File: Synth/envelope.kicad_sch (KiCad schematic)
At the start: 20 parts, among them U10 LM321, U7 LM321, U8 LM321, U9 LM321

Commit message: added some footprints
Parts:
- C5, C6: value C_Small -> 1uF; footprint (none) -> Capacitor_SMD:C_0805_2012Metric
- D1: value D -> 100k; footprint (none) -> Diode_SMD:D_0805_2012Metric
- D2, D3, D4, D5: footprint (none) -> Diode_SMD:D_0805_2012Metric
- R19: value R -> 10k; footprint (none) -> Resistor_SMD:R_0805_2012Metric
- R20, R21, R23: value R -> 100k; footprint (none) -> Resistor_SMD:R_0805_2012Metric
- R22: value R -> 47k; footprint (none) -> Resistor_SMD:R_0805_2012Metric
- R24: value R -> 1k; footprint (none) -> Resistor_SMD:R_0805_2012Metric
- RV10: value R_Potentiometer -> 1M
- RV9: value R_Potentiometer -> 100k
- renumbered RV11 to 1M1
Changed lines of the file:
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@@
   (symbol (lib_id "Device:R_Potentiometer") (at 175.26 108.585 270) (unit 1)
     (in_bom yes) (on_board yes) (dnp no)
-    (property "Reference" "RV11" (at 175.26 102.235 90)
+    (property "Reference" "1M1" (at 175.26 102.235 90)
       (effects (font (size 1.27 1.27)))
     )
@@
       (project "Synth"
         (path "/69caad27-d98a-4cdc-abd0-794bd5e6ba79/f75ed15d-dc0c-437e-bd82-524bc7e88f27"
-          (reference "RV11") (unit 1)
+          (reference "1M1") (unit 1)
         )
       )
@@
       (effects (font (size 1.27 1.27)))
     )
-    (property "Footprint" "" (at 167.64 108.585 0)
+    (property "Footprint" "Diode_SMD:D_0805_2012Metric" (at 167.64 108.585 0)
       (effects (font (size 1.27 1.27)) hide)
     )
@@
   (symbol (lib_id "Device:R_Potentiometer") (at 132.08 126.365 90) (unit 1)
     (in_bom yes) (on_board yes) (dnp no) (fields_autoplaced)
-    (property "Reference" "RV9" (at 132.08 130.175 90)
-      (effects (font (size 1.27 1.27)))
-    )
-    (property "Value" "R_Potentiometer" (at 132.08 132.715 90)
+    (property "Reference" "RV9" (at 132.08 129.54 90)
+      (effects (font (size 1.27 1.27)))
+    )
+    (property "Value" "100k" (at 132.08 132.08 90)
       (effects (font (size 1.27 1.27)))
     )
@@
       (effects (font (size 1.27 1.27)) (justify left))
     )
-    (property "Value" "R" (at 69.85 102.235 0)
+    (property "Value" "10k" (at 69.85 102.235 0)
       (effects (font (size 1.27 1.27)) (justify left))
     )
-    (property "Footprint" "" (at 66.167 100.965 90)
+    (property "Footprint" "Resistor_SMD:R_0805_2012Metric" (at 66.167 100.965 90)
       (effects (font (size 1.27 1.27)) hide)
     )
@@
       (effects (font (size 1.27 1.27)))
     )
-    (property "Value" "R" (at 89.535 114.935 90)
-      (effects (font (size 1.27 1.27)))
-    )
-    (property "Footprint" "" (at 89.535 114.173 90)
+    (property "Value" "100k" (at 89.535 114.935 90)
+      (effects (font (size 1.27 1.27)))
+    )
+    (property "Footprint" "Resistor_SMD:R_0805_2012Metric" (at 89.535 114.173 90)
       (effects (font (size 1.27 1.27)) hide)
     )
@@
       (effects (font (size 1.27 1.27)) (justify right))
     )
-    (property "Value" "C_Small" (at 198.12 102.8636 0)
+    (property "Value" "1uF" (at 198.12 102.8636 0)
       (effects (font (size 1.27 1.27)) (justify right))
     )
-    (property "Footprint" "" (at 195.58 101.6 0)
+    (property "Footprint" "Capacitor_SMD:C_0805_2012Metric" (at 195.58 101.6 0)
       (effects (font (size 1.27 1.27)) hide)
     )
@@
       (effects (font (size 1.27 1.27)))
     )
-    (property "Footprint" "" (at 123.19 98.425 0)
+    (property "Footprint" "Diode_SMD:D_0805_2012Metric" (at 123.19 98.425 0)
       (effects (font (size 1.27 1.27)) hide)
     )
@@
   (symbol (lib_id "Device:R") (at 106.68 112.395 90) (unit 1)
     (in_bom yes) (on_board yes) (dnp no) (fields_autoplaced)
-    (property "Reference" "R22" (at 106.68 106.045 90)
-      (effects (font (size 1.27 1.27)))
-    )
-    (property "Value" "R" (at 106.68 108.585 90)
-      (effects (font (size 1.27 1.27)))
-    )
-    (property "Footprint" "" (at 106.68 114.173 90)
+    (property "Reference" "R22" (at 106.68 106.68 90)
+      (effects (font (size 1.27 1.27)))
+    )
+    (property "Value" "47k" (at 106.68 109.22 90)
+      (effects (font (size 1.27 1.27)))
+    )
+    (property "Footprint" "Resistor_SMD:R_0805_2012Metric" (at 106.68 114.173 90)
       (effects (font (size 1.27 1.27)) hide)
     )
@@
       (effects (font (size 1.27 1.27)))
     )
-    (property "Footprint" "" (at 123.19 126.365 0)
+    (property "Footprint" "Diode_SMD:D_0805_2012Metric" (at 123.19 126.365 0)
       (effects (font (size 1.27 1.27)) hide)
     )
@@
       (effects (font (size 1.27 1.27)))
     )
-    (property "Footprint" "" (at 167.64 83.185 0)
+    (property "Footprint" "Diode_SMD:D_0805_2012Metric" (at 167.64 83.185 0)
       (effects (font (size 1.27 1.27)) hide)
     )
@@
   (symbol (lib_id "Device:D") (at 76.835 95.885 180) (unit 1)
     (in_bom yes) (on_board yes) (dnp no) (fields_autoplaced)
-    (property "Reference" "D1" (at 76.835 89.535 0)
-      (effects (font (size 1.27 1.27)))
-    )
-    (property "Value" "D" (at 76.835 92.075 0)
-      (effects (font (size 1.27 1.27)))
-    )
-    (property "Footprint" "" (at 76.835 95.885 0)
+    (property "Reference" "D1" (at 76.835 90.17 0)
+      (effects (font (size 1.27 1.27)))
+    )
+    (property "Value" "100k" (at 76.835 92.71 0)
+      (effects (font (size 1.27 1.27)))
+    )
+    (property "Footprint" "Diode_SMD:D_0805_2012Metric" (at 76.835 95.885 0)
       (effects (font (size 1.27 1.27)) hide)
     )
@@
   (symbol (lib_id "Device:R") (at 227.965 92.71 270) (unit 1)
     (in_bom yes) (on_board yes) (dnp no) (fields_autoplaced)
-    (property "Reference" "R24" (at 227.965 86.995 90)
-      (effects (font (size 1.27 1.27)))
-    )
-    (property "Value" "R" (at 227.965 89.535 90)
-      (effects (font (size 1.27 1.27)))
-    )
-    (property "Footprint" "" (at 227.965 90.932 90)
+    (property "Reference" "R24" (at 227.965 86.36 90)
+      (effects (font (size 1.27 1.27)))
+    )
+    (property "Value" "1k" (at 227.965 88.9 90)
+      (effects (font (size 1.27 1.27)))
+    )
+    (property "Footprint" "Resistor_SMD:R_0805_2012Metric" (at 227.965 90.932 90)
       (effects (font (size 1.27 1.27)) hide)
     )
@@
   (symbol (lib_id "Device:R_Potentiometer") (at 175.26 83.185 90) (unit 1)
     (in_bom yes) (on_board yes) (dnp no) (fields_autoplaced)
-    (property "Reference" "RV10" (at 175.26 86.995 90)
-      (effects (font (size 1.27 1.27)))
-    )
-    (property "Value" "R_Potentiometer" (at 175.26 89.535 90)
+    (property "Reference" "RV10" (at 175.26 86.36 90)
+      (effects (font (size 1.27 1.27)))
+    )
+    (property "Value" "1M" (at 175.26 88.9 90)
       (effects (font (size 1.27 1.27)))
     )
@@
   (symbol (lib_id "Device:R") (at 83.82 100.965 0) (unit 1)
     (in_bom yes) (on_board yes) (dnp no) (fields_autoplaced)
-    (property "Reference" "R20" (at 85.725 99.695 0)
+    (property "Reference" "R20" (at 86.36 99.695 0)
       (effects (font (size 1.27 1.27)) (justify left))
     )
-    (property "Value" "R" (at 85.725 102.235 0)
+    (property "Value" "100k" (at 86.36 102.235 0)
       (effects (font (size 1.27 1.27)) (justify left))
     )
-    (property "Footprint" "" (at 82.042 100.965 90)
+    (property "Footprint" "Resistor_SMD:R_0805_2012Metric" (at 82.042 100.965 90)
       (effects (font (size 1.27 1.27)) hide)
     )
@@
   (symbol (lib_id "Device:C_Small") (at 60.325 95.885 90) (unit 1)
     (in_bom yes) (on_board yes) (dnp no) (fields_autoplaced)
-    (property "Reference" "C5" (at 60.3313 89.535 90)
-      (effects (font (size 1.27 1.27)))
-    )
-    (property "Value" "C_Small" (at 60.3313 92.075 90)
-      (effects (font (size 1.27 1.27)))
-    )
-    (property "Footprint" "" (at 60.325 95.885 0)
+    (property "Reference" "C5" (at 60.3313 88.9 90)
+      (effects (font (size 1.27 1.27)))
+    )
+    (property "Value" "1uF" (at 60.3313 91.44 90)
+      (effects (font (size 1.27 1.27)))
+    )
+    (property "Footprint" "Capacitor_SMD:C_0805_2012Metric" (at 60.325 95.885 0)
       (effects (font (size 1.27 1.27)) hide)
     )
@@
       (effects (font (size 1.27 1.27)) (justify left))
     )
-    (property "Value" "R" (at 134.62 113.03 0)
+    (property "Value" "100k" (at 134.62 113.03 0)
       (effects (font (size 1.27 1.27)) (justify left))
     )
-    (property "Footprint" "" (at 130.302 111.76 90)
-      (effects (font (size 1.27 1.27)) hide)
-    )
+    (property "Footprint" "Resistor_SMD:R_0805_2012Metric" (at 130.302 111.76 90)
+      (effects (font (size 1.27 1.27)) hide)
+    )

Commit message: add the layout
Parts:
- 1M1, RV10: footprint (none) -> Potentiometer_THT:Potentiometer_Bourns_PTV09A-1_Single_Vertical
- RV9: footprint (none) -> Resistor_SMD:R_0805_2012Metric
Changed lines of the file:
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@@
       (effects (font (size 1.27 1.27)))
     )
-    (property "Footprint" "" (at 175.26 108.585 0)
+    (property "Footprint" "Potentiometer_THT:Potentiometer_Bourns_PTV09A-1_Single_Vertical" (at 175.26 108.585 0)
       (effects (font (size 1.27 1.27)) hide)
     )
@@
       (effects (font (size 1.27 1.27)))
     )
-    (property "Footprint" "" (at 132.08 126.365 0)
+    (property "Footprint" "Resistor_SMD:R_0805_2012Metric" (at 132.08 126.365 0)
       (effects (font (size 1.27 1.27)) hide)
     )
@@
       (effects (font (size 1.27 1.27)))
     )
-    (property "Footprint" "" (at 175.26 83.185 0)
-      (effects (font (size 1.27 1.27)) hide)
-    )
+    (property "Footprint" "Potentiometer_THT:Potentiometer_Bourns_PTV09A-1_Single_Vertical" (at 175.26 83.185 0)
+      (effects (font (size 1.27 1.27)) hide)
+    )

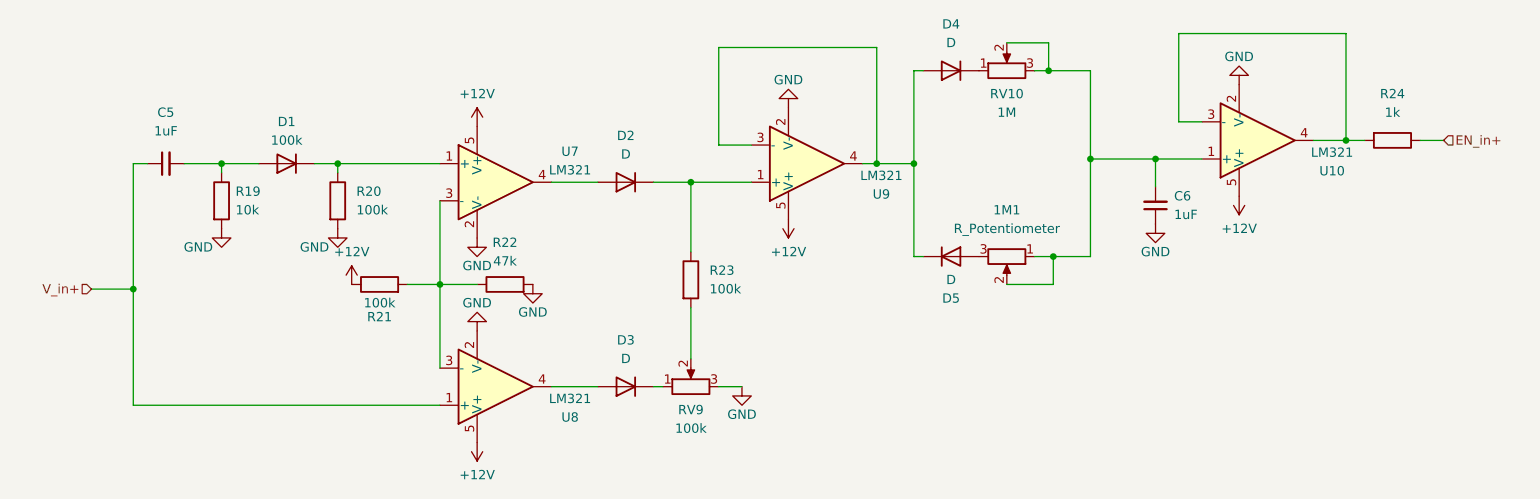
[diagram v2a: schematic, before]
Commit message: fixed erc errs
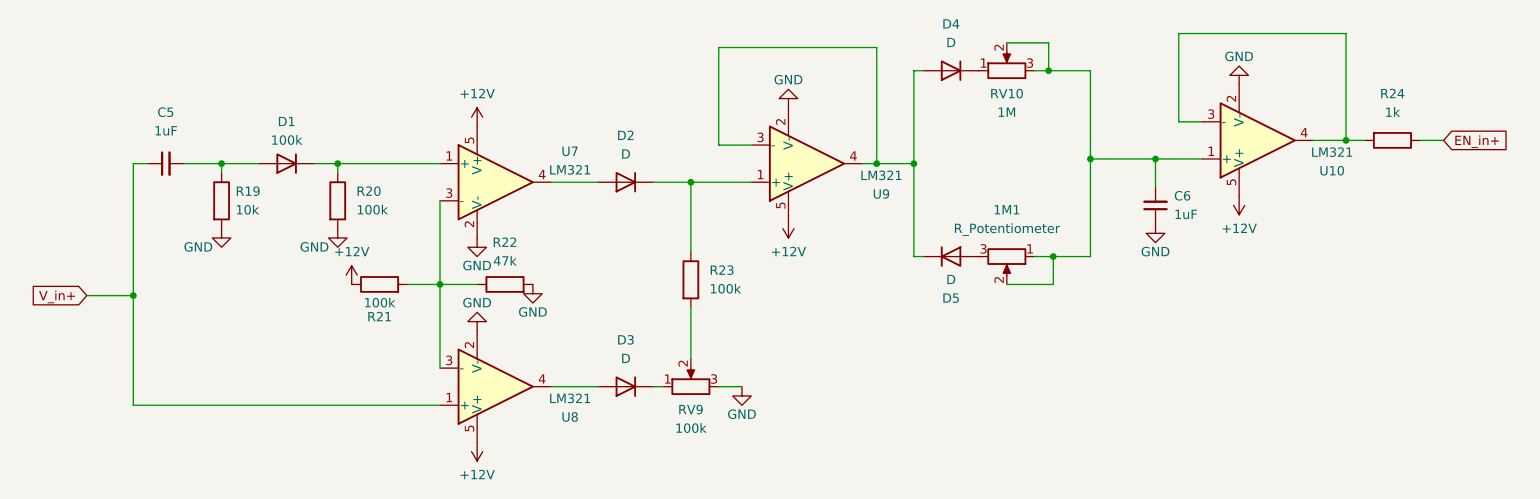
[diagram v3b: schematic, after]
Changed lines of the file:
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@@
   (junction (at 132.08 98.425) (diameter 0) (color 0 0 0 0)
-  )
-  (junction (at 55.88 113.03) (diameter 0) (color 0 0 0 0)
   )
   (junction (at 97.79 112.395) (diameter 0) (color 0 0 0 0)
@@
   (junction (at 195.58 95.25) (diameter 0) (color 0 0 0 0)
   )
+  (junction (at 55.88 113.919) (diameter 0) (color 0 0 0 0)
+  )
   (junction (at 186.69 95.25) (diameter 0) (color 0 0 0 0)
   )
@@
     (stroke (width 0) (type default))
   )
-  (wire (pts (xy 50.165 113.03) (xy 55.88 113.03))
+  (wire (pts (xy 49.53 113.919) (xy 55.88 113.919))
     (stroke (width 0) (type default))
   )
@@
     (stroke (width 0) (type default))
   )
+  (wire (pts (xy 55.88 113.919) (xy 55.88 128.905))
+    (stroke (width 0) (type default))
+  )
   (wire (pts (xy 186.69 95.25) (xy 186.69 108.585))
     (stroke (width 0) (type default))
@@
     (stroke (width 0) (type default))
   )
-  (wire (pts (xy 55.88 95.885) (xy 55.88 113.03))
-    (stroke (width 0) (type default))
-  )
   (wire (pts (xy 231.775 92.71) (xy 234.95 92.71))
     (stroke (width 0) (type default))
@@
     (stroke (width 0) (type default))
   )
-  (wire (pts (xy 55.88 113.03) (xy 55.88 128.905))
+  (wire (pts (xy 55.88 95.885) (xy 55.88 113.919))
     (stroke (width 0) (type default))
   )
@@
     (stroke (width 0) (type default))
   )
-  (hierarchical_label "V_in+" (shape input) (at 50.165 113.03 180) (fields_autoplaced)
+  (global_label "V_in+" (shape input) (at 49.53 113.919 180) (fields_autoplaced)
     (effects (font (size 1.27 1.27)) (justify right))
+    (property "Intersheetrefs" "${INTERSHEET_REFS}" (at 41.1624 113.919 0)
+      (effects (font (size 1.27 1.27)) (justify right) hide)
+    )
   )
-  (hierarchical_label "EN_in+" (shape input) (at 234.95 92.71 0) (fields_autoplaced)
+  (global_label "EN_in+" (shape input) (at 234.95 92.71 0) (fields_autoplaced)
     (effects (font (size 1.27 1.27)) (justify left))
+    (property "Intersheetrefs" "${INTERSHEET_REFS}" (at 244.7085 92.71 0)
+      (effects (font (size 1.27 1.27)) (justify left) hide)
+    )
   )
   (symbol (lib_id "Device:R_Potentiometer") (at 175.26 108.585 270) (unit 1)

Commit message: changed the potentiometer footprints
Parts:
- RV10: footprint Potentiometer_THT:Potentiometer_Bourns_PTV09A-1_Single_Vertical -> Potentiometer_THT:Potentiometer_Bourns_3299W_Vertical
- RV9: footprint Resistor_SMD:R_0805_2012Metric -> Potentiometer_THT:Potentiometer_Bourns_3299W_Vertical
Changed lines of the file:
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@@
       (effects (font (size 1.27 1.27)))
     )
-    (property "Footprint" "Resistor_SMD:R_0805_2012Metric" (at 132.08 126.365 0)
+    (property "Footprint" "Potentiometer_THT:Potentiometer_Bourns_3299W_Vertical" (at 132.08 126.365 0)
       (effects (font (size 1.27 1.27)) hide)
     )
@@
       (effects (font (size 1.27 1.27)))
     )
-    (property "Footprint" "Potentiometer_THT:Potentiometer_Bourns_PTV09A-1_Single_Vertical" (at 175.26 83.185 0)
-      (effects (font (size 1.27 1.27)) hide)
-    )
+    (property "Footprint" "Potentiometer_THT:Potentiometer_Bourns_3299W_Vertical" (at 175.26 83.185 0)
+      (effects (font (size 1.27 1.27)) hide)
+    )

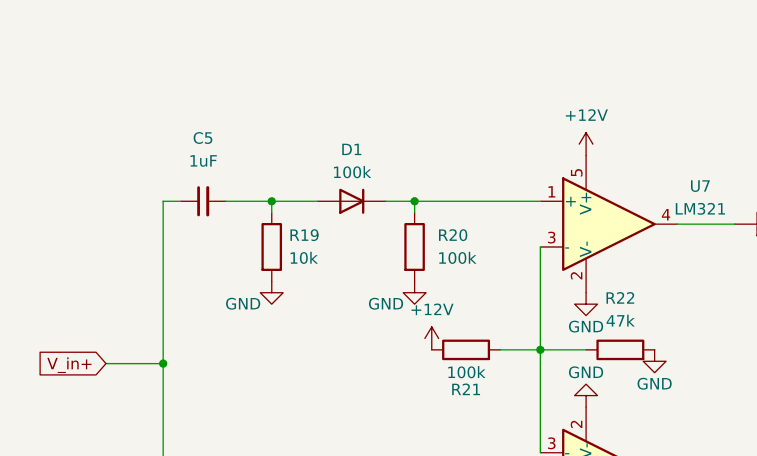
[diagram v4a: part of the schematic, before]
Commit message: made small changes, fixed DRC Errors
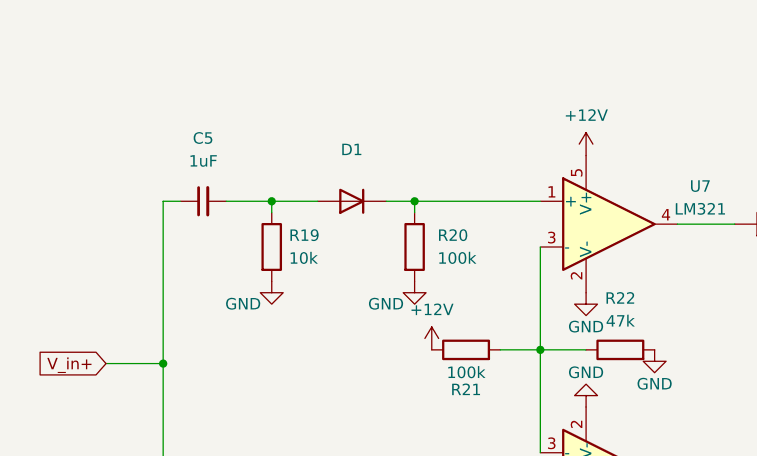
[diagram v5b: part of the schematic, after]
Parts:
- D1: value 100k -> (none)
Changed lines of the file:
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@@
       (effects (font (size 1.27 1.27)))
     )
-    (property "Value" "100k" (at 76.835 92.71 0)
+    (property "Value" "" (at 76.835 92.71 0)
       (effects (font (size 1.27 1.27)))
     )

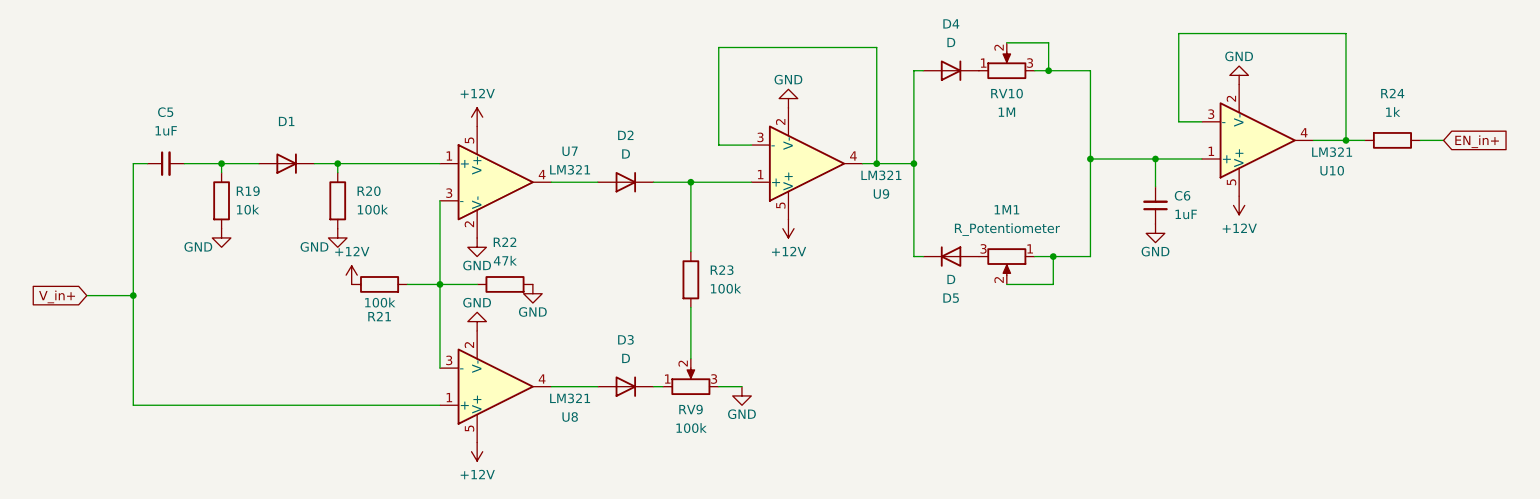
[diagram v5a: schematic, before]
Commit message: changed hierarchical labels
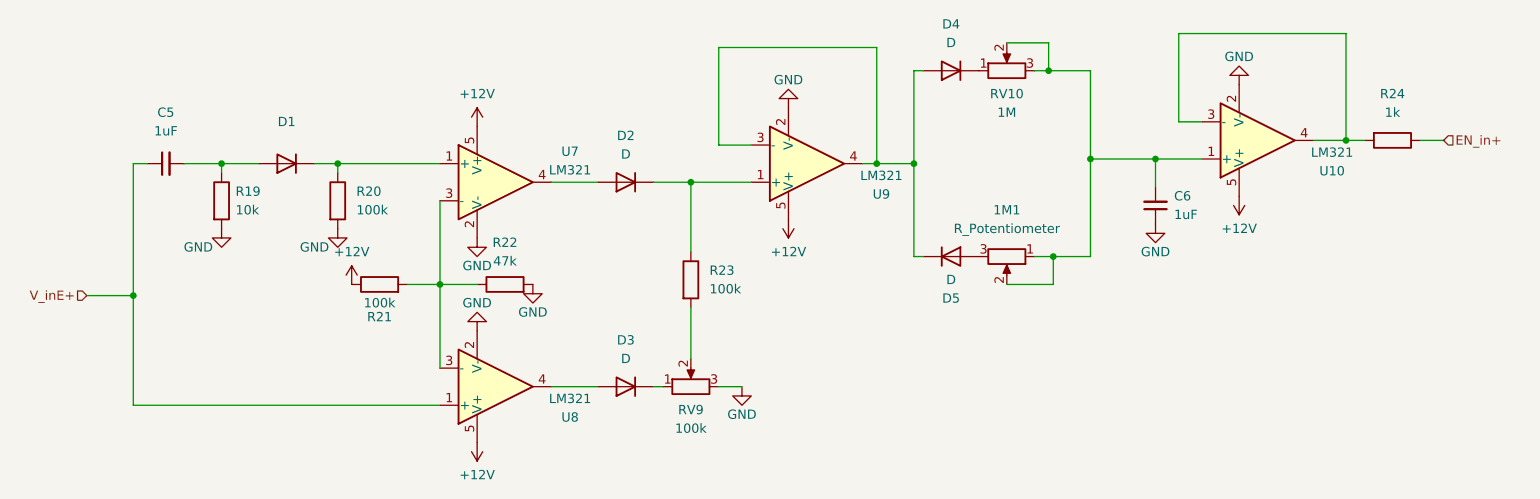
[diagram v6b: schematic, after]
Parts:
- D1: value (none) -> ~
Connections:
- net V_in+ renamed V_inE+
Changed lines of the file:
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@@
     (stroke (width 0) (type default))
   )
-  (global_label "V_in+" (shape input) (at 49.53 113.919 180) (fields_autoplaced)
+  (hierarchical_label "EN_in+" (shape input) (at 234.95 92.71 0) (fields_autoplaced)
+    (effects (font (size 1.27 1.27)) (justify left))
+  )
+  (hierarchical_label "V_inE+" (shape input) (at 49.53 113.919 180) (fields_autoplaced)
     (effects (font (size 1.27 1.27)) (justify right))
-    (property "Intersheetrefs" "${INTERSHEET_REFS}" (at 41.1624 113.919 0)
-      (effects (font (size 1.27 1.27)) (justify right) hide)
-    )
-  )
-  (global_label "EN_in+" (shape input) (at 234.95 92.71 0) (fields_autoplaced)
-    (effects (font (size 1.27 1.27)) (justify left))
-    (property "Intersheetrefs" "${INTERSHEET_REFS}" (at 244.7085 92.71 0)
-      (effects (font (size 1.27 1.27)) (justify left) hide)
-    )
   )
   (symbol (lib_id "Device:R_Potentiometer") (at 175.26 108.585 270) (unit 1)
@@
       (effects (font (size 1.27 1.27)))
     )
-    (property "Value" "" (at 76.835 92.71 0)
-      (effects (font (size 1.27 1.27)))
-    )
+    (property "Value" "~" (at 76.835 92.71 0)
+      (effects (font (size 1.27 1.27)))
+    )
